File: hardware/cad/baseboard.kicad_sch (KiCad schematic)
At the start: 11 parts, among them U101 LT3580xDD

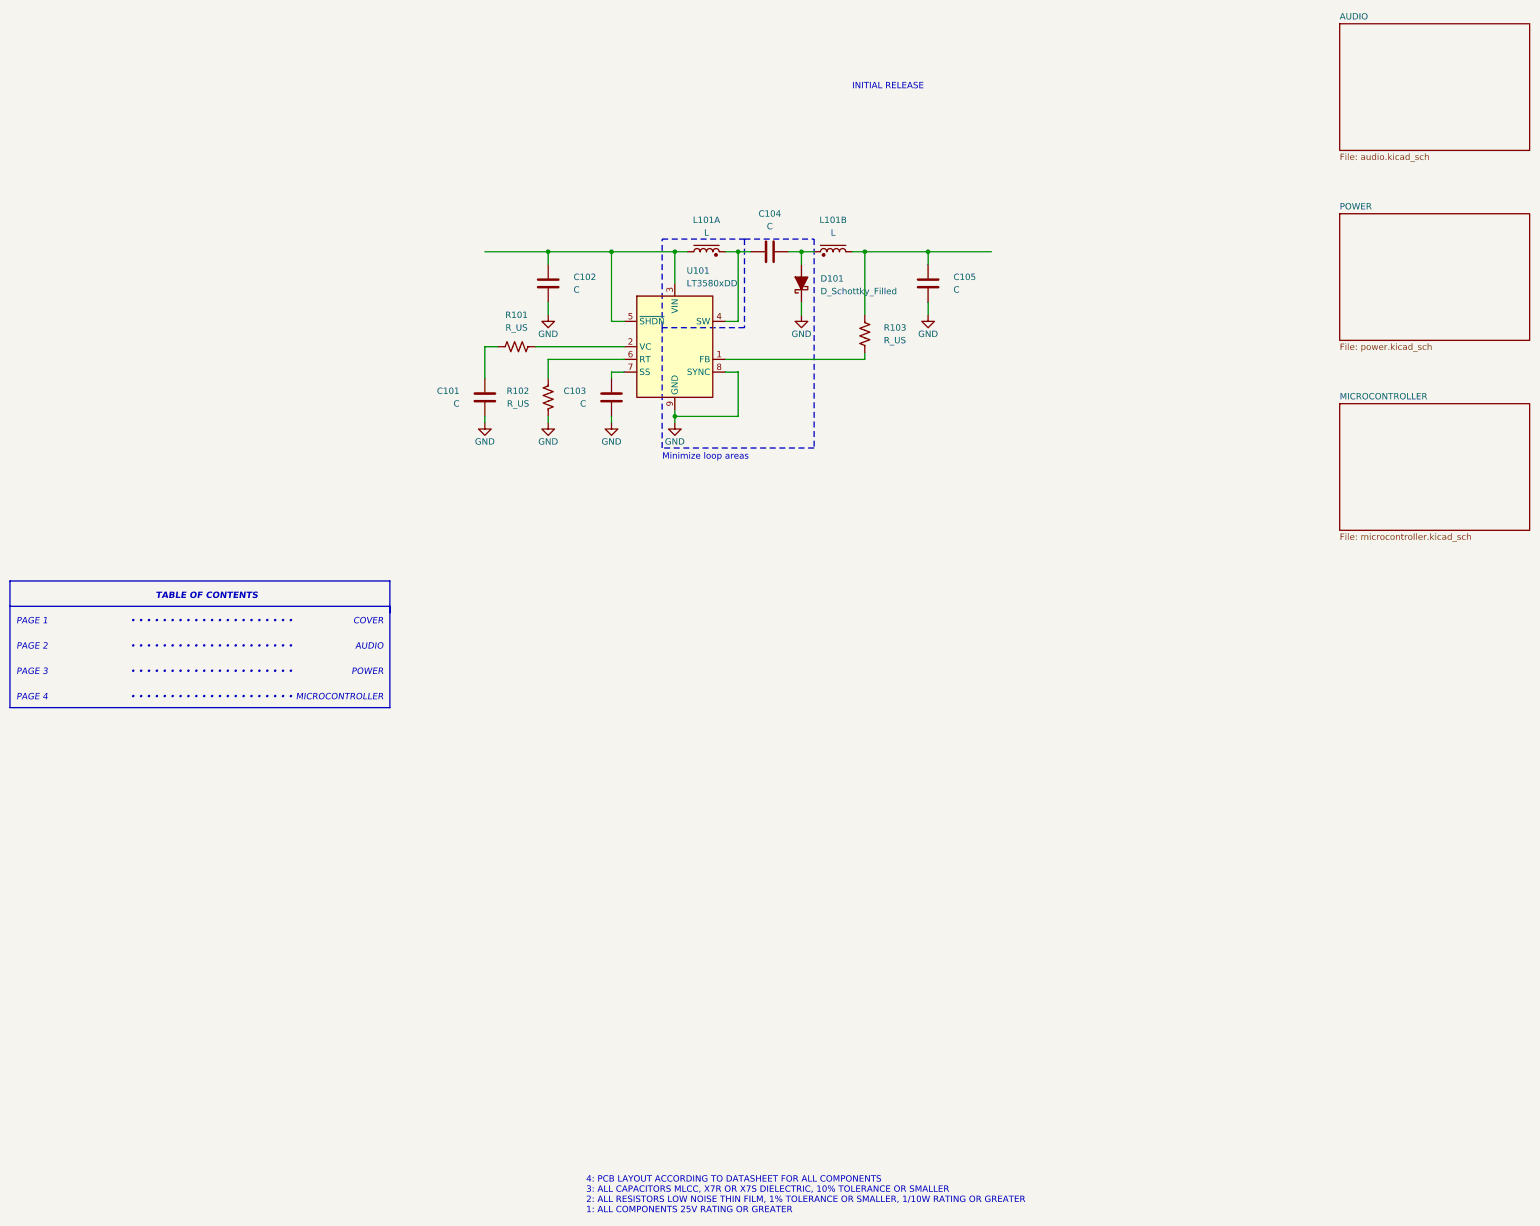
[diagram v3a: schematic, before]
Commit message: minor changes before moving to new power supply topology
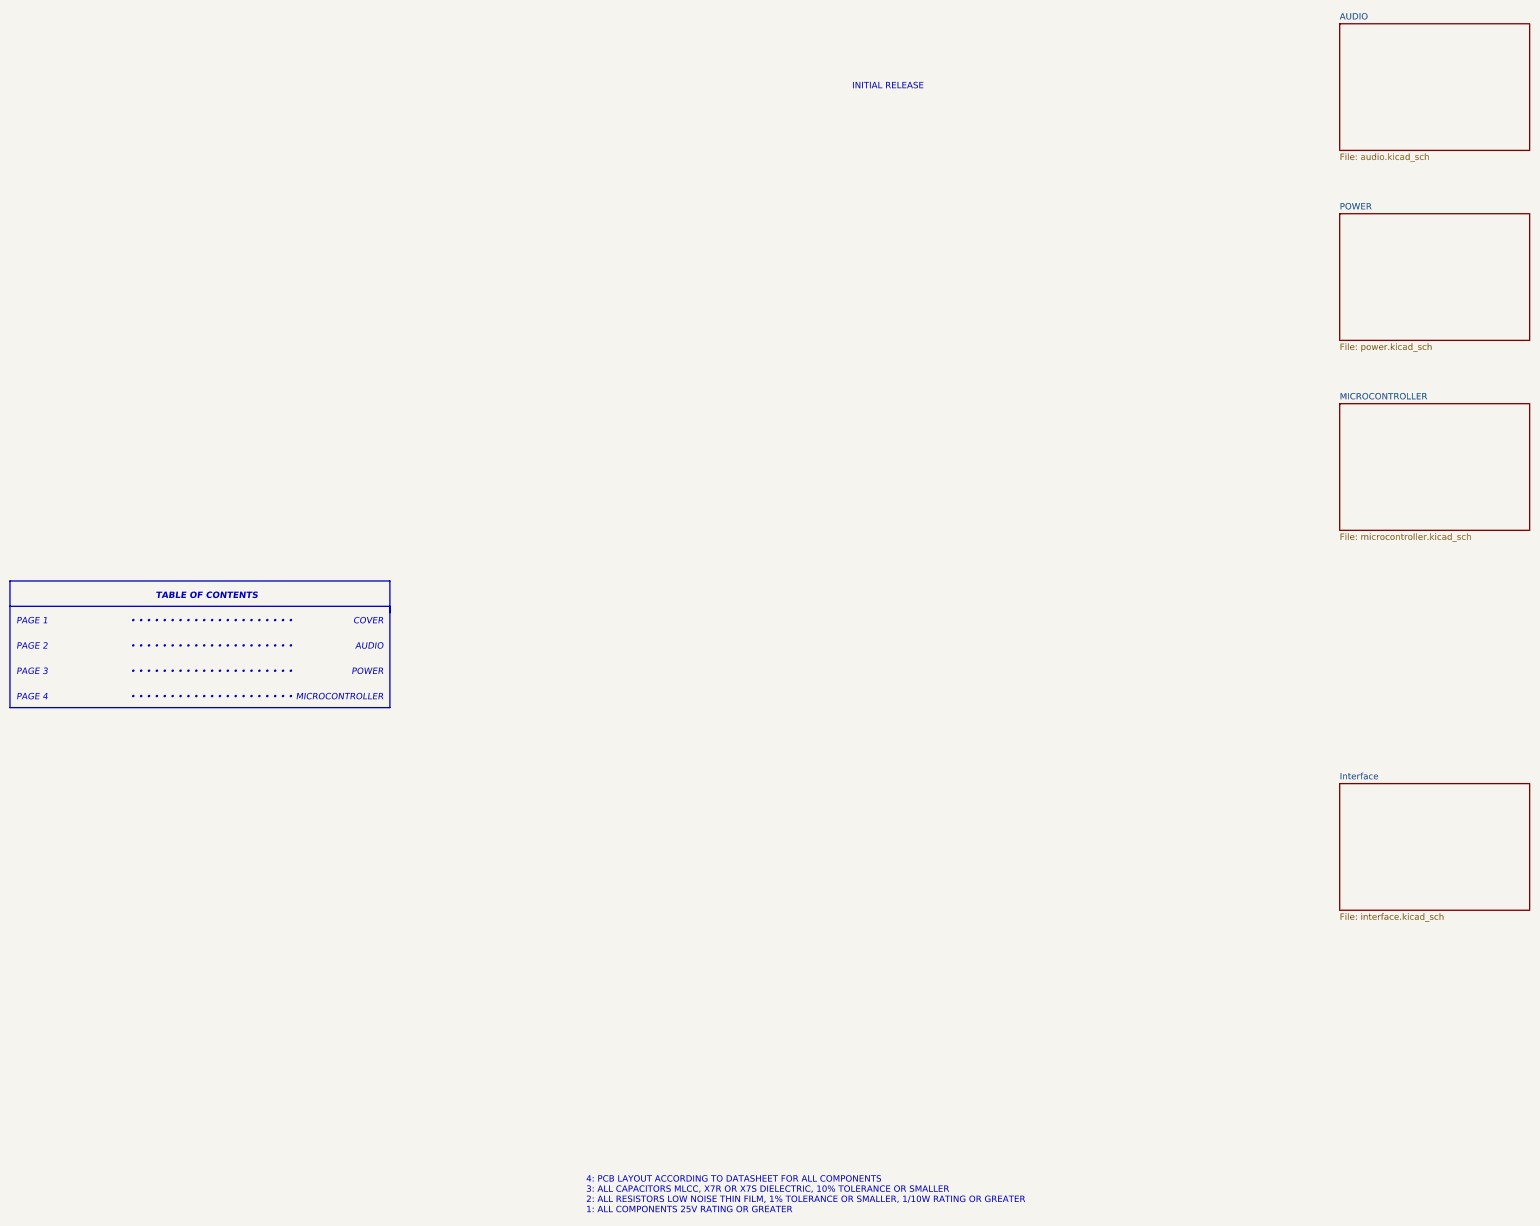
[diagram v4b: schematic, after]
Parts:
- removed C101, C102, C103, C104, C105: C, symbol Device:C
- removed D101: D_Schottky_Filled, symbol Device:D_Schottky_Filled
- removed L101: L, symbol Library:L_Coupled_POLAR
- removed R101, R102, R103: R_US, symbol Device:R_US
- removed U101: LT3580xDD, Package_DFN_QFN:DFN-8-1EP_3x3mm_P0.5mm_EP1.66x2.38mm, symbol Regulator_Switching:LT3580xDD
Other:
- added sheet Interface (interface.kicad_sch)
- note removed: "Minimize loop areas"

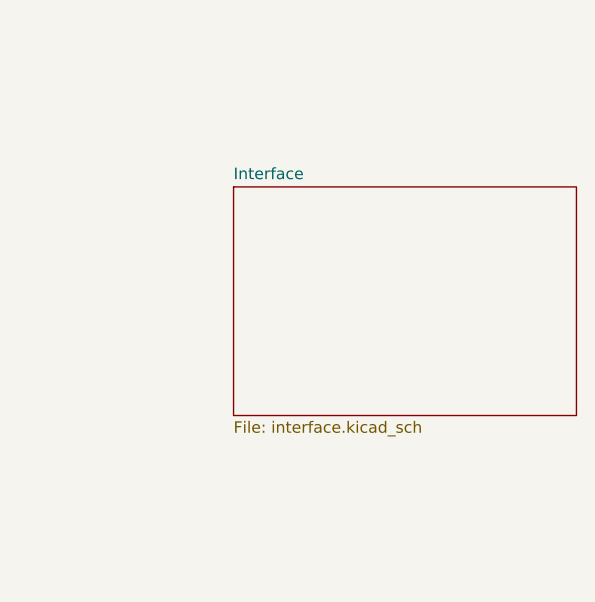
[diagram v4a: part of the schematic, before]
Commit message: started modeling circuits
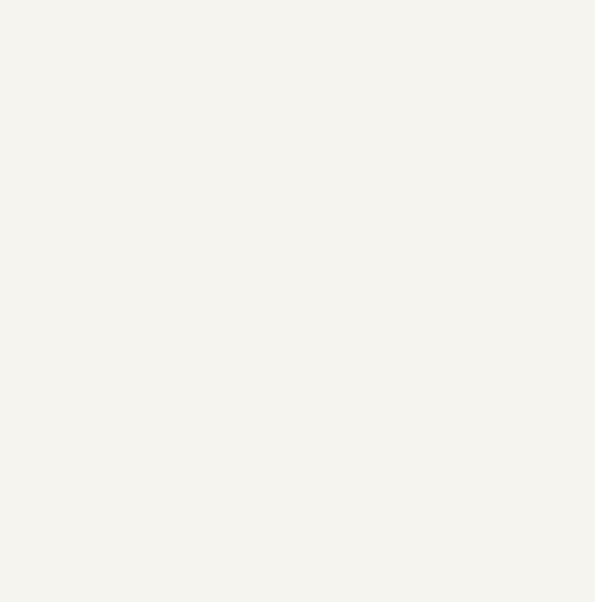
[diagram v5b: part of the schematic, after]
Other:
- removed sheet Interface
